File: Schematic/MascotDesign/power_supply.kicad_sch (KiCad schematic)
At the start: 7 parts, among them J1 Charger input, J11 Main power cutoff (soldered s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, J2 PI power USB, J3 LCD LED Power, U1 Generic_Buck_Regulator, U2 Generic_Buck_Regulator

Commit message: Slight PCB tweaking
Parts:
- removed J3: LCD LED Power, Connector_PinHeader_2.54mm:PinHeader_2x03_P2.54mm_Vertical, symbol Connector_Generic:Conn_02x03_Odd_Even
- added J3: LCD LED Power, Connector_PinHeader_2.54mm:PinHeader_2x04_P2.54mm_Vertical, symbol Connector_Generic:Conn_02x04_Odd_Even
- J1: footprint Connector_PinHeader_2.54mm:PinHeader_1x02_P2.54mm_Vertical -> Connector_JST:JST_XH_B2B-XH-A_1x02_P2.50mm_Vertical
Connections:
- net GND: now also J3.2 (Pin_2), J3.4 (Pin_4), J3.6 (Pin_6), J3.8 (Pin_8)
- net LCD 5v5: now also J3.1 (Pin_1), J3.3 (Pin_3), J3.5 (Pin_5), J3.7 (Pin_7)
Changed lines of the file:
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@@
+	)
+	(junction
+		(at 80.01 72.39)
+		(diameter 0)
+		(color 0 0 0 0)
+	)
+	(junction
+		(at 85.09 36.83)
+		(diameter 0)
+		(color 0 0 0 0)
+	)
+	(junction
+		(at 48.26 41.91)
+		(diameter 0)
+		(color 0 0 0 0)
+	)
+	(junction
+		(at 147.32 44.45)
+		(diameter 0)
+		(color 0 0 0 0)
+	)
+	(junction
+		(at 81.28 40.64)
+		(diameter 0)
+		(color 0 0 0 0)
+	)
+	(junction
+		(at 147.32 41.91)
+		(diameter 0)
+		(color 0 0 0 0)
+	)
+	(junction
+		(at 132.08 36.83)
+		(diameter 0)
+		(color 0 0 0 0)
+	)
+	(junction
+		(at 39.37 34.29)
+		(diameter 0)
+		(color 0 0 0 0)
+	)
+	(junction
+		(at 147.32 39.37)
+		(diameter 0)
+		(color 0 0 0 0)
+	)
+	(junction
+		(at 77.47 36.83)
+		(diameter 0)
+		(color 0 0 0 0)
+	)
+	(junction
+		(at 132.08 41.91)
+		(diameter 0)
+		(color 0 0 0 0)
 	)
 	(junction
 		(at 132.08 39.37)
-		(diameter 0)
-		(color 0 0 0 0)
-	)
-	(junction
-		(at 80.01 72.39)
-		(diameter 0)
-		(color 0 0 0 0)
-	)
-	(junction
-		(at 85.09 36.83)
-		(diameter 0)
-		(color 0 0 0 0)
-	)
-	(junction
-		(at 48.26 41.91)
-		(diameter 0)
-		(color 0 0 0 0)
-	)
-	(junction
-		(at 81.28 40.64)
-		(diameter 0)
-		(color 0 0 0 0)
-	)
-	(junction
-		(at 147.32 41.91)
-		(diameter 0)
-		(color 0 0 0 0)
-	)
-	(junction
-		(at 39.37 34.29)
-		(diameter 0)
-		(color 0 0 0 0)
-	)
-	(junction
-		(at 147.32 39.37)
-		(diameter 0)
-		(color 0 0 0 0)
-	)
-	(junction
-		(at 77.47 36.83)
-		(diameter 0)
-		(color 0 0 0 0)
-	)
-	(junction
-		(at 132.08 36.83)
 		(diameter 0)
 		(color 0 0 0 0)
@@
 	(wire
 		(pts
+			(xy 132.08 41.91) (xy 132.08 44.45)
+		)
+		(stroke
+			(width 0)
+			(type default)
+		)
+	)
+	(wire
+		(pts
 			(xy 55.88 31.75) (xy 55.88 34.29)
 		)
@@
 	(wire
 		(pts
+			(xy 132.08 39.37) (xy 132.08 41.91)
+		)
+		(stroke
+			(width 0)
+			(type default)
+		)
+	)
+	(wire
+		(pts
 			(xy 113.03 30.48) (xy 113.03 36.83)
 		)
@@
 	(wire
 		(pts
-			(xy 148.59 41.91) (xy 147.32 41.91)
-		)
-		(stroke
-			(width 0)
-			(type default)
-		)
-	)
-	(wire
-		(pts
-			(xy 132.08 39.37) (xy 132.08 41.91)
+			(xy 148.59 44.45) (xy 147.32 44.45)
 		)
 		(stroke
@@
 	(wire
 		(pts
+			(xy 144.78 44.45) (xy 147.32 44.45)
+		)
+		(stroke
+			(width 0)
+			(type default)
+		)
+	)
+	(wire
+		(pts
 			(xy 81.28 54.61) (xy 81.28 40.64)
 		)
@@
 		(pts
 			(xy 144.78 36.83) (xy 147.32 36.83)
+		)
+		(stroke
+			(width 0)
+			(type default)
+		)
+	)
+	(wire
+		(pts
+			(xy 147.32 44.45) (xy 147.32 41.91)
 		)
 		(stroke
@@
 			)
 		)
-		(property "Footprint" "Connector_PinHeader_2.54mm:PinHeader_1x02_P2.54mm_Vertical"
+		(property "Footprint" "Connector_JST:JST_XH_B2B-XH-A_1x02_P2.50mm_Vertical"
 			(at 55.88 26.67 0)
 			(effects
@@
 	)
 	(symbol
-		(lib_id "Connector_Generic:Conn_02x03_Odd_Even")
+		(lib_id "Connector_Generic:Conn_02x04_Odd_Even")
 		(at 137.16 39.37 0)
 		(unit 1)
@@
 			)
 		)
-		(property "Footprint" "Connector_PinHeader_2.54mm:PinHeader_2x03_P2.54mm_Vertical"
+		(property "Footprint" "Connector_PinHeader_2.54mm:PinHeader_2x04_P2.54mm_Vertical"
 			(at 137.16 39.37 0)
 			(effects
@@
 			)
 		)
-		(property "Description" "Generic connector, double row, 02x03, odd/even pin numbering scheme (row 1 odd numbers, row 2 even numbers), script generated (kicad-library-utils/schlib/autogen/connector/)"
+		(property "Description" "Generic connector, double row, 02x04, odd/even pin numbering scheme (row 1 odd numbers, row 2 even numbers), script generated (kicad-library-utils/schlib/autogen/connector/)"
 			(at 137.16 39.37 0)
 			(effects
@@
 			)
 		)
+		(pin "6"
+		)
+		(pin "2"
+		)
+		(pin "8"
+		)
 		(pin "1"
 		)
-		(pin "2"
-		)
-		(pin "6"
+		(pin "3"
+		)
+		(pin "5"
 		)
 		(pin "4"
 		)
-		(pin "3"
-		)
-		(pin "5"
+		(pin "7"
 		)
 		(instances
-			(project "MascotDesign"
+			(project ""
 				(path "/ba045f6c-d730-41b1-992e-d77c9aee61c5/621dc98a-3a96-4433-a17f-2055bce50a9c"
 					(reference "J3")
@@
 	(symbol
 		(lib_id "power:GND")
-		(at 148.59 41.91 90)
+		(at 148.59 44.45 90)
 		(unit 1)
 		(exclude_from_sim no)
@@
 		(fields_autoplaced yes)
 		(property "Reference" "#PWR07"
-			(at 154.94 41.91 0)
+			(at 154.94 44.45 0)
 			(effects
 				(font
@@
 		)
 		(property "Value" "GND"
-			(at 152.4 41.9099 90)
+			(at 152.4 44.4499 90)
 			(effects
 				(font
@@
 		)
 		(property "Footprint" ""
-			(at 148.59 41.91 0)
+			(at 148.59 44.45 0)
 			(effects
 				(font
@@
 		)
 		(property "Datasheet" ""
-			(at 148.59 41.91 0)
+			(at 148.59 44.45 0)
 			(effects
 				(font
@@
 		)
 		(property "Description" "Power symbol creates a global label with name \"GND\" , ground"
-			(at 148.59 41.91 0)
-			(effects
-				(font
+			(at 148.59 44.45 0)
+			(effects
+				(font

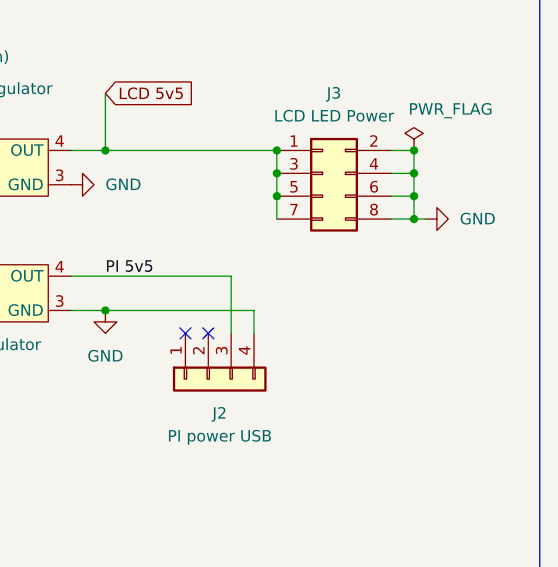
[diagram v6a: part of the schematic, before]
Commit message: Finalize and order PCB
Ordered through JLC, so formatting was exported to match that
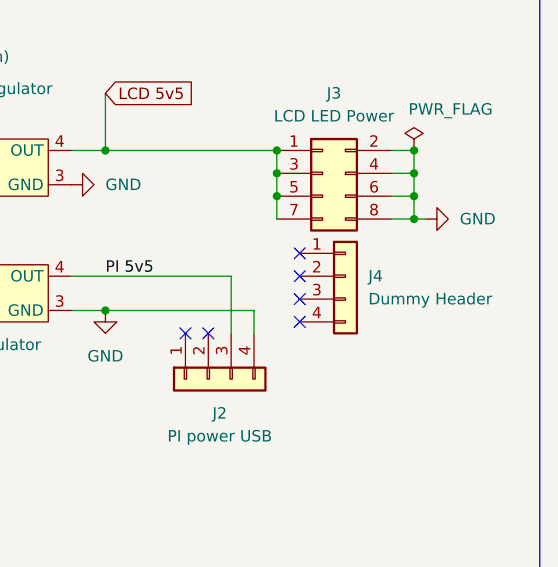
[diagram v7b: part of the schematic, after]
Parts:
- added J4: Dummy Header, Connector_PinHeader_2.54mm:PinHeader_1x04_P2.54mm_Vertical, symbol Connector_Generic:Conn_01x04
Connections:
- no-connect marks 2 -> 6
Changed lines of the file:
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@@
+	)
+	(no_connect
+		(at 134.62 53.34)
+	)
+	(no_connect
+		(at 134.62 50.8)
+	)
+	(no_connect
+		(at 134.62 55.88)
 	)
 	(no_connect
 		(at 124.46 57.15)
+	)
+	(no_connect
+		(at 134.62 48.26)
 	)
 	(no_connect
@@
 					(unit 1)
 				)
+			)
+		)
+	)
+	(symbol
+		(lib_id "Connector_Generic:Conn_01x04")
+		(at 139.7 50.8 0)
+		(unit 1)
+		(exclude_from_sim no)
+		(in_bom yes)
+		(on_board yes)
+		(dnp no)
+		(fields_autoplaced yes)
+		(property "Reference" "J4"
+			(at 142.24 50.7999 0)
+			(effects
+				(font
+					(size 1.27 1.27)
+				)
+				(justify left)
+			)
+		)
+		(property "Value" "Dummy Header"
+			(at 142.24 53.3399 0)
+			(effects
+				(font
+					(size 1.27 1.27)
+				)
+				(justify left)
+			)
+		)
+		(property "Footprint" "Connector_PinHeader_2.54mm:PinHeader_1x04_P2.54mm_Vertical"
+			(at 139.7 50.8 0)
+			(effects
+				(font
+					(size 1.27 1.27)
+				)
+				(hide yes)
+			)
+		)
+		(property "Datasheet" "~"
+			(at 139.7 50.8 0)
+			(effects
+				(font
+					(size 1.27 1.27)
+				)
+				(hide yes)
+			)
+		)
+		(property "Description" "Generic connector, single row, 01x04, script generated (kicad-library-utils/schlib/autogen/connector/)"
+			(at 139.7 50.8 0)
+			(effects
+				(font
+					(size 1.27 1.27)
+				)
+				(hide yes)
+			)
+		)
+		(pin "4"
+		)
+		(pin "2"
+		)
+		(pin "3"
+		)
+		(pin "1"
+		)
+		(instances
+			(project ""
+				(path "/ba045f6c-d730-41b1-992e-d77c9aee61c5/621dc98a-3a96-4433-a17f-2055bce50a9c"
+					(reference "J4")
+					(unit 1)
+				)
